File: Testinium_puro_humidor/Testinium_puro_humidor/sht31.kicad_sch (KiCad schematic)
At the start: 0 parts

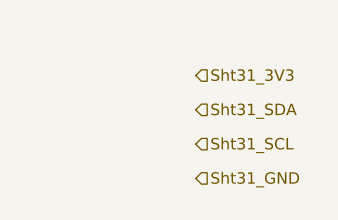
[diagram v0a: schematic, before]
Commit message: fan , uv led ,regülator devresi eklendi. piezo ve sarj devresi kaldi
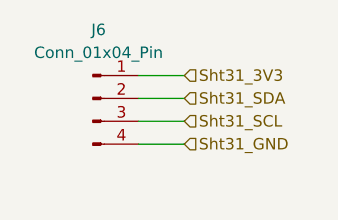
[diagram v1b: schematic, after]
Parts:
- added J6: Conn_01x04_Pin, Connector_JST:JST_EH_B4B-EH-A_1x04_P2.50mm_Vertical, symbol Connector:Conn_01x04_Pin
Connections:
- net Sht31_3V3: now also J6.1 (Pin_1)
- net Sht31_GND: now also J6.4 (Pin_4)
- net Sht31_SCL: now also J6.3 (Pin_3)
- net Sht31_SDA: now also J6.2 (Pin_2)
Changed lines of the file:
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@@
 	(generator_version "9.0")
 	(paper "A4")
+	(wire
+		(pts
+			(xy 39.37 43.18) (xy 34.29 43.18)
+		)
+		(stroke
+			(width 0)
+			(type default)
+		)
+	)
+	(wire
+		(pts
+			(xy 39.37 35.56) (xy 34.29 35.56)
+		)
+		(stroke
+			(width 0)
+			(type default)
+		)
+	)
+	(wire
+		(pts
+			(xy 39.37 38.1) (xy 34.29 38.1)
+		)
+		(stroke
+			(width 0)
+			(type default)
+		)
+	)
+	(wire
+		(pts
+			(xy 39.37 40.64) (xy 34.29 40.64)
+		)
+		(stroke
+			(width 0)
+			(type default)
+		)
+	)
 	(hierarchical_label "Sht31_SDA"
 		(shape input)
-		(at 40.64 39.37 0)
+		(at 39.37 38.1 0)
 		(effects
 			(font
@@
 	(hierarchical_label "Sht31_SCL"
 		(shape input)
-		(at 40.64 43.18 0)
+		(at 39.37 40.64 0)
 		(effects
 			(font
@@
 	(hierarchical_label "Sht31_GND"
 		(shape input)
-		(at 40.64 46.99 0)
+		(at 39.37 43.18 0)
 		(effects
 			(font
@@
 	(hierarchical_label "Sht31_3V3"
 		(shape input)
-		(at 40.64 35.56 0)
+		(at 39.37 35.56 0)
 		(effects
 			(font
@@
 		)
 	)
+	(symbol
+		(lib_id "Connector:Conn_01x04_Pin")
+		(at 29.21 38.1 0)
+		(unit 1)
+		(exclude_from_sim no)
+		(in_bom yes)
+		(on_board yes)
+		(dnp no)
+		(fields_autoplaced yes)
+		(property "Reference" "J6"
+			(at 29.845 30.48 0)
+			(effects
+				(font
+					(size 1.27 1.27)
+				)
+			)
+		)
+		(property "Value" "Conn_01x04_Pin"
+			(at 29.845 33.02 0)
+			(effects
+				(font
+					(size 1.27 1.27)
+				)
+			)
+		)
+		(property "Footprint" "Connector_JST:JST_EH_B4B-EH-A_1x04_P2.50mm_Vertical"
+			(at 29.21 38.1 0)
+			(effects
+				(font
+					(size 1.27 1.27)
+				)
+				(hide yes)
+			)
+		)
+		(property "Datasheet" "~"
+			(at 29.21 38.1 0)
+			(effects
+				(font
+					(size 1.27 1.27)
+				)
+				(hide yes)
+			)
+		)
+		(property "Description" "Generic connector, single row, 01x04, script generated"
+			(at 29.21 38.1 0)
+			(effects
+				(font
+					(size 1.27 1.27)
+				)
+				(hide yes)
+			)
+		)
+		(pin "4"
+		)
+		(pin "1"
+		)
+		(pin "2"
+		)
+		(pin "3"
+		)
+		(instances
+			(project ""
+				(path "/eaf24445-473d-4e1b-a90d-ef2c4a02e74f/c1bc02f1-56ff-4a8f-b982-d269aa1d4f4c"
+					(reference "J6")
+					(unit 1)
+				)
+			)
+		)
+	)

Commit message: sematik tamamlandi
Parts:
- added R27: 0R, Resistor_SMD:R_0603_1608Metric, symbol Device:R
- J6: value Conn_01x04_Pin -> Conn_Sht31
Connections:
- net Sht31_3V3: no longer names the net of J6.1 (Pin_1)
- net Sht31_3V3: now also R27.2
- net Sht31_GND renamed GND
- new net 5V: R27.1
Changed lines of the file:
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@@
 	(wire
 		(pts
-			(xy 39.37 35.56) (xy 34.29 35.56)
+			(xy 41.91 35.56) (xy 43.18 35.56)
 		)
 		(stroke
@@
 			(width 0)
 			(type default)
+		)
+	)
+	(global_label "5V"
+		(shape input)
+		(at 43.18 35.56 0)
+		(fields_autoplaced yes)
+		(effects
+			(font
+				(size 1.27 1.27)
+			)
+			(justify left)
+		)
+		(property "Intersheetrefs" "${INTERSHEET_REFS}"
+			(at 48.4633 35.56 0)
+			(effects
+				(font
+					(size 1.27 1.27)
+				)
+				(justify left)
+				(hide yes)
+			)
 		)
 	)
@@
 		)
 	)
-	(hierarchical_label "Sht31_GND"
-		(shape input)
-		(at 39.37 43.18 0)
-		(effects
-			(font
-				(size 1.27 1.27)
-			)
-			(justify left)
-		)
-	)
-	(hierarchical_label "Sht31_3V3"
-		(shape input)
-		(at 39.37 35.56 0)
-		(effects
-			(font
-				(size 1.27 1.27)
-			)
-			(justify left)
+	(symbol
+		(lib_id "Device:R")
+		(at 38.1 35.56 270)
+		(unit 1)
+		(exclude_from_sim no)
+		(in_bom yes)
+		(on_board yes)
+		(dnp no)
+		(property "Reference" "R27"
+			(at 38.1 38.1 90)
+			(effects
+				(font
+					(size 1.27 1.27)
+				)
+			)
+		)
+		(property "Value" "0R"
+			(at 38.1 35.56 90)
+			(effects
+				(font
+					(size 1.27 1.27)
+				)
+			)
+		)
+		(property "Footprint" "Resistor_SMD:R_0603_1608Metric"
+			(at 38.1 33.782 90)
+			(effects
+				(font
+					(size 1.27 1.27)
+				)
+				(hide yes)
+			)
+		)
+		(property "Datasheet" "~"
+			(at 38.1 35.56 0)
+			(effects
+				(font
+					(size 1.27 1.27)
+				)
+				(hide yes)
+			)
+		)
+		(property "Description" "Resistor"
+			(at 38.1 35.56 0)
+			(effects
+				(font
+					(size 1.27 1.27)
+				)
+				(hide yes)
+			)
+		)
+		(property "HHH" ""
+			(at 38.1 35.56 0)
+			(effects
+				(font
+					(size 1.27 1.27)
+				)
+				(hide yes)
+			)
+		)
+		(pin "1"
+		)
+		(pin "2"
+		)
+		(instances
+			(project "Testinium_puro_humidor"
+				(path "/eaf24445-473d-4e1b-a90d-ef2c4a02e74f/c1bc02f1-56ff-4a8f-b982-d269aa1d4f4c"
+					(reference "R27")
+					(unit 1)
+				)
+			)
 		)
 	)
@@
 			)
 		)
-		(property "Value" "Conn_01x04_Pin"
+		(property "Value" "Conn_Sht31"
 			(at 29.845 33.02 0)
 			(effects
@@
 					(unit 1)
 				)
+			)
+		)
+	)
+	(symbol
+		(lib_id "power:GND")
+		(at 39.37 43.18 0)
+		(unit 1)
+		(exclude_from_sim no)
+		(in_bom yes)
+		(on_board yes)
+		(dnp no)
+		(fields_autoplaced yes)
+		(property "Reference" "#PWR010"
+			(at 39.37 49.53 0)
+			(effects
+				(font
+					(size 1.27 1.27)
+				)
+				(hide yes)
+			)
+		)
+		(property "Value" "GND"
+			(at 39.37 48.26 0)
+			(effects
+				(font
+					(size 1.27 1.27)
+				)
+			)
+		)
+		(property "Footprint" ""
+			(at 39.37 43.18 0)
+			(effects
+				(font
+					(size 1.27 1.27)
+				)
+				(hide yes)
+			)
+		)
+		(property "Datasheet" ""
+			(at 39.37 43.18 0)
+			(effects
+				(font
+					(size 1.27 1.27)
+				)
+				(hide yes)
+			)
+		)
+		(property "Description" "Power symbol creates a global label with name \"GND\" , ground"
+			(at 39.37 43.18 0)
+			(effects
+				(font
+					(size 1.27 1.27)
+				)
+				(hide yes)
+			)
+		)
+		(pin "1"
+		)
+		(instances
+			(project "Testinium_puro_humidor"
+				(path "/eaf24445-473d-4e1b-a90d-ef2c4a02e74f/c1bc02f1-56ff-4a8f-b982-d269aa1d4f4c"
+					(reference "#PWR010")
+					(unit 1)
+				)
